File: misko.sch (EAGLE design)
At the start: 48 parts, among them IC1 MC1525TT, IC2 FT230XS, U1 ATMEGA1281-16AU, U2 SN74HCT14DR, U3 SN74LVC1G3157DBVR - BT switch, U4 SN74LVC1G3157DBVR - GPS switch, U5 TMP36GRTZ-REEL7, U6 TPS63030DSKT, U7 MCP73871-2AAI/ML

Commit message: - further work on eagle schematic
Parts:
- added C10: 0.47µF, resistor:C-EUC0805
- added C11, C13: 10µF, resistor:C-EUC0805
- added G1: CR2450V, battery:CR2450V
- added NTC: 10k, rcl:R-EU_R0805
- added R22, R23, R24, R25, R28, R31, R33, R34, R35: 1k, rcl:R-EU_R0805
- added R26, R29, R30: 47k, rcl:R-EU_R0805
- added R27: 270k, rcl:R-EU_R0805
- added R32: 100k, rcl:R-EU_R0805
- added S7: up, switch-omron:10-XX
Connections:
- removed net N$1: IC1.GND
- removed net N$12: U5.GND
- new net AREF: IC1.VO, U1.AREF
- new net AVCC: U1.AVCC
- new net N$11: R23.2, R24.1, U7.VPCC
- new net N$13: C13.1, G1.+, R34.1, U7.VBAT, U7.VBAT_2, U7.VBAT_SENSE
- new net N$18: R28.1, U7.THERM
- new net N$19: R27.1, R28.2
- new net N$20: NTC.1, R27.2
- new net N$22: R31.1, U7.PROG1
- new net N$23: R32.1, U7.PROG3
- new net RESET: U1.~RESET
- new net XTAL1: U1.XTAL1
- new net XTAL2: U1.XTAL2
- net BAT_A_PIN: now also R33.1, R34.2, U1.PF2_(ADC2); no longer U1.PF3_(ADC3)
- net GND: now also C11.2, C13.2, G1.-, IC1.GND, NTC.2, R24.2, R31.2, R32.2, R33.2, R35.2, U5.GND, U7.VSS, U7.VSS_2
- net MCP73871_CHARGE_STATUS_1_PIN: now also R30.2, U7.STAT1/*LBO
- net MCP73871_CHARGE_STATUS_2_PIN: now also R29.2, U7.STAT2
- net MCP73871_POWER_GOOD_PIN: now also R26.2, U7.*PG
- net VCC: now also C11.1, R23.1, R25.1, R26.1, R29.1, R30.1, U7.*TE, U7.CE, U7.IN, U7.IN_2, U7.OUT, U7.OUT_2, U7.PROG2, U7.SEL
- net VCC_SENSE_PIN: now also R25.2, R35.1
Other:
- note added: "Analog Switch"
- note added: "Motherboard"
- note added: "Power Supply"
- note added: "Temperature Sensor"
- note added: "Vcc Measurement"
- note added: "Voltage Reference"
- moved on the sheet: C1, IC1, LED1, LED2, R1, R5, U1, U3, U4, U5, U6, U7

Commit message: - further porting of schematic to eagle
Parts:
- removed S7: up, switch-omron:10-XX
- added C12: 4.7µF, resistor:C-EUC0805
- added C14: 0.1µF, resistor:C-EUC0805
- added S8: SWS001, smd-special:SWS001
- C10: value 0.47µF -> 10µF
- R22, R33, R34: value 1k -> 150k
- R23: value 1k -> 100k
- R24: value 1k -> 270k
- R25, R35: value 1k -> 200k
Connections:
- new net N$1: R22.1, S8.1, U6.EN
- new net N$12: U7.IN
- new net N$15: U7.SEL
- new net N$24: U7.PROG2
- new net N$25: U7.*TE
- new net N$26: U7.CE
- new net N$28: R17.1, R20.1, S5.S, S5.S1
- new net N$29: R16.1, R19.1, S6.S, S6.S1
- new net N$30: R18.1, R21.1, S4.S, S4.S1
- new net VBAT: C11.1, C12.2, S8.2, U6.PS/SYNC, U6.VIN, U6.VINA, U7.OUT, U7.OUT_2
- net 5V0: now also R23.1, U7.IN_2
- net GND: now also C10.1, C12.1, C14.2, R22.2, U6.GND, U6.PGND; no longer R16.1, R17.1, R18.1, R19.1, R21.1, S4.S, S4.S1, S5.S, S5.S1, S6.S, S6.S1
- net VCC: now also C10.2, C14.1, U6.FB, U6.VOUT; no longer C11.1, R23.1, U7.*TE, U7.CE, U7.IN, U7.IN_2, U7.OUT, U7.OUT_2, U7.PROG2, U7.SEL
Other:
- note added: "Power Supply - Buck/Boost Regulator"
- note added: "Power Supply - Power Path Controller"
- note added: "USB to Serial"
- note removed: "Power Supply"
- moved on the sheet: C1, C10, C11, C13, C2, C3, C4, C5, C6, C7, C8, C9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

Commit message: - further work on eagle schematic
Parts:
- removed C1: (no value), resistor:C-EUC1206
- removed G1: CR2450V, battery:CR2450V
- removed R1: (no value), resistor:R-EU_R1206
- added CN1: (no value), SIM800C:JST_2PIN-SMT
- added G2: CR2450V, battery:CR2450V
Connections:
- removed net N$13: C13.1, G1.+, R34.1, U7.VBAT, U7.VBAT_2, U7.VBAT_SENSE
- removed net N$24: U7.PROG2
- removed net N$25: U7.*TE
- removed net N$26: U7.CE
- new net VBAT+: C13.1, CN1.1, G2.+, R34.1, U7.VBAT, U7.VBAT_2, U7.VBAT_SENSE
- net GND: now also CN1.2, G2.-; no longer G1.-
- net N$15: now also U7.*TE, U7.CE, U7.PROG2
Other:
- moved on the sheet: R29, R30

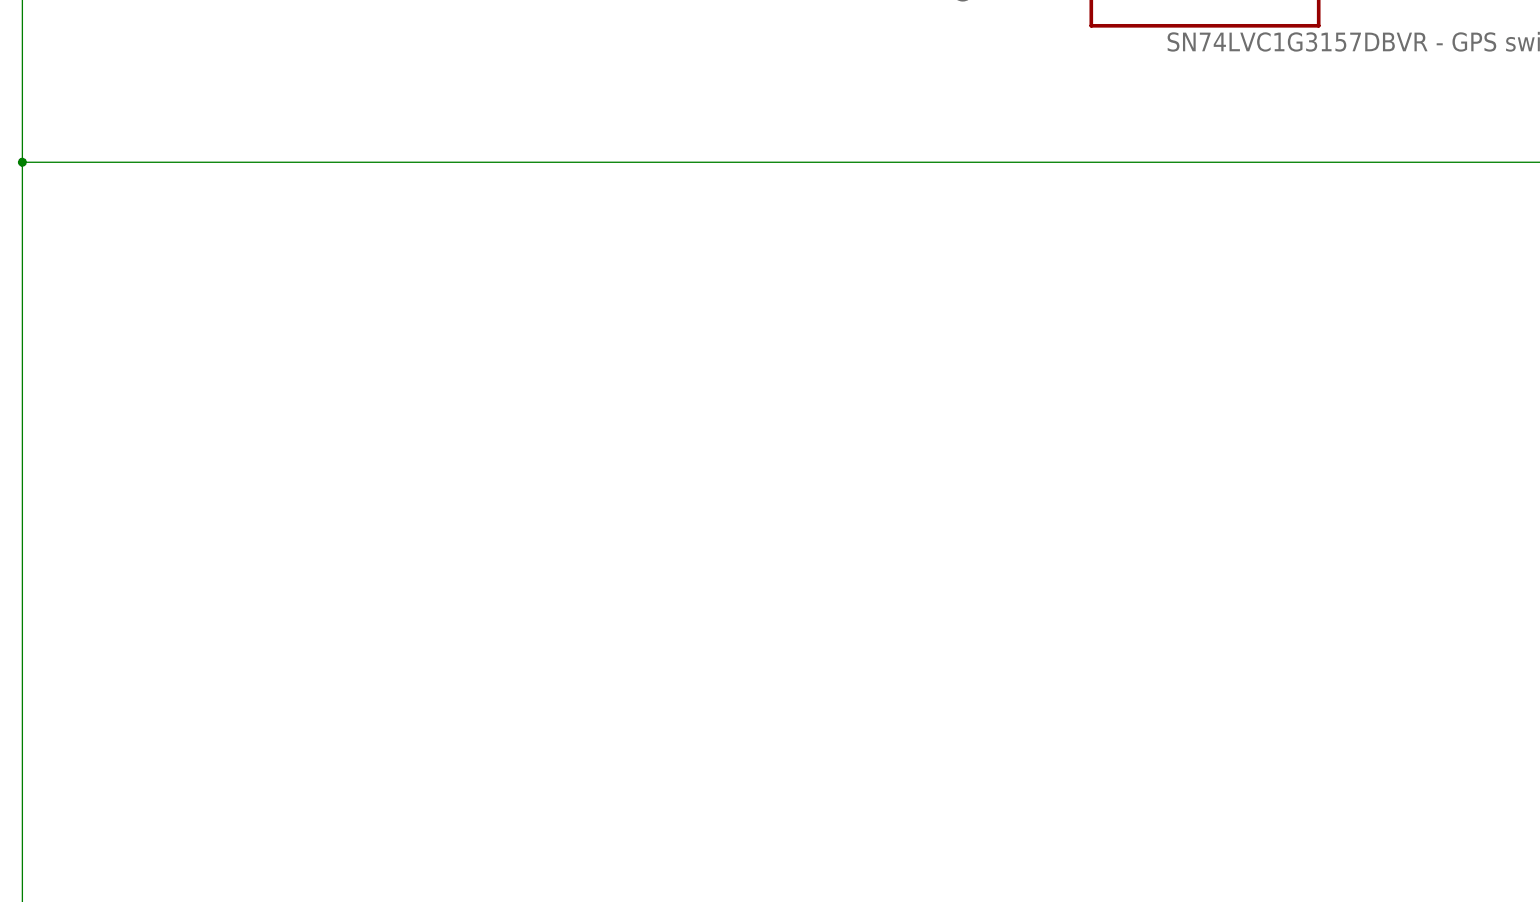
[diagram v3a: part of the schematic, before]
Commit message: - added ADXL345 Accelerometer.lbr, WIP
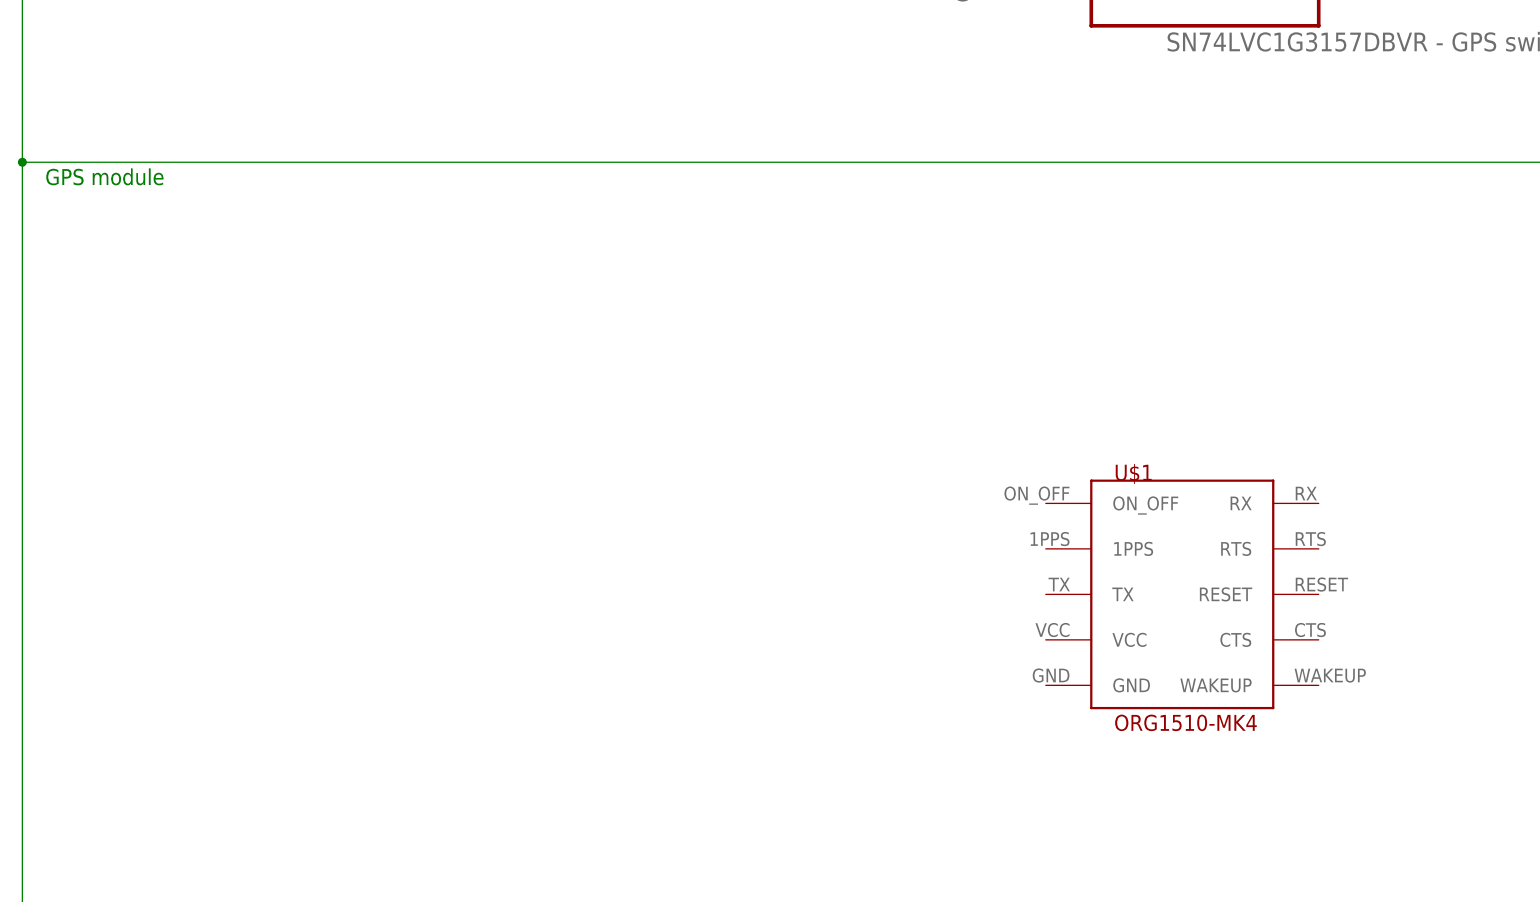
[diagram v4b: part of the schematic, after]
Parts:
- added U$1: ORG1510-MK4, ORG1510-MK4 GPS module:ORG1510-MK4
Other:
- note added: "GPS module"
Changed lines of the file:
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@@
 <setting verticaltext="up"/>
 </settings>
-<grid distance="0.1" unitdist="inch" unit="inch" style="lines" multiple="1" display="no" altdistance="0.01" altunitdist="inch" altunit="inch"/>
+<grid distance="0.1" unitdist="inch" unit="inch" style="lines" multiple="1" display="yes" altdistance="0.01" altunitdist="inch" altunit="inch"/>
 <layers>
 <layer number="1" name="Top" color="4" fill="1" visible="no" active="no"/>
@@
 <part name="CN1" library="SIM800C" deviceset="JST_2PIN" device="-SMT"/>
 <part name="G2" library="battery" deviceset="CR2450V" device=""/>
+<part name="U$1" library="ORG1510-MK4 GPS module" deviceset="ORG1510-MK4" device=""/>
 </parts>
 <sheets>
@@
 <text x="134.62" y="553.72" size="1.778" layer="91">Power Supply - Power Path Controller</text>
 <text x="5.08" y="320.04" size="1.778" layer="91">USB to Serial</text>
+<text x="2.54" y="99.06" size="1.778" layer="91">GPS module</text>
 </plain>
 <instances>
@@
 <instance part="CN1" gate="G$1" x="320.04" y="510.54"/>
 <instance part="G2" gate="1" x="274.32" y="480.06" rot="R90"/>
+<instance part="U$1" gate="G$1" x="119.38" y="40.64"/>
 </instances>
 <busses>

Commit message: - added two datasheets
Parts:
- added ANT1: (no value), discrete:ANTENNA
- added C1: 1µF, resistor:C-EUC1206
- added C15: 18pF, resistor:C-EUC1206
- added C16: 18pF, rcl:C-EUC0805
- added C17, C21, C26: 0.1µF, rcl:C-EUC0805
- added C18: 1F, rcl:C-EUC0805
- added C19, C20: 100µF, rcl:C-EUC0805
- added C22, C29: 0.1µF, resistor:C-EUC0805
- added C23, C24: 15pF, resistor:C-EUC0805
- added C25, C27, C28: 10µF, rcl:C-EUC0805
- added C30: 100nF, resistor:C-EUC1206
- added D1: 1N4148, Diode2:1N4148
- added IC3: LTC4425, LTC4425 Supercap Charger:LTC4425
- added IC4: FM25W256-SOIC, FM25W256 FERAM:FM25W256-SOIC
- added IC5: (no value), 74HCT1G32GW:74HCT1G32GW-DC
- added L1: DJNR6045-100-S, DJNR6045-100S Power Inductor:DJNR6045-100-S
- added L2: 33µH, rcl:L-US
- added L3: 1.5µH, inductor-neosid:MS50
- added LED4, LED6: red, led:LEDSML1206
- added LED5: green, led:LEDSML1206
- added Q1: FDN304P, transistor-power:N-HEXFET-2D_SOT232-IRLL014N
- added Q2: 8MHz, crystal:CRYTALHC33U-V
- added R1: 220, resistor:R-EU_R1206
- added R36, R42, R43, R44: 10k, resistor:R-EU_R1206
- added R37, R38: 100k, resistor:R-EU_R1206
- added R39, R41, R48, R50, R52: 1k, resistor:R-EU_R1206
- added R40: 46k, resistor:R-EU_R1206
- added R45, R46: 270k, rcl:R-EU_R0805
- added R47: 47k, rcl:R-EU_R0805
- added R49: 4.7k, rcl:R-EU_R0805
- added R51: 47k, resistor:R-EU_R1206
- added S7: left, switch-omron:10-XX
- added SJ1, SJ2: (no value), jumper:SJW
- added SV1: (no value), con-lstb:MA05-2
- added SV2: (no value), con-lstb:MA04-1
- added U$2: ORG1510-MK4, ORG1510-MK4 GPS module:ORG1510-MK4
- added U$3: RN-42, EN42-I Bluetooth Module:RN-42
- added U$4: ADXL345, ADXL345 Accelerometer:ADXL345
- added X1: MINI-USB_4P-32005-101, con-cypressindustries:MINI-USB_4P-32005-101
- added X2: SIM-CARD_496191611, con-molex:SIM-CARD_496191611
- added X3: SDBMF, farnell:SDBMF
- C6: value 0.1µF -> 10µF; device resistor:C-EUC0805 -> rcl:C-EUC0805
- LED1: value (none) -> blue
- R14: value 21 -> 100k; device rcl:R-EU_R0805 -> resistor:R-EU_R1206
- R15: value 21 -> 1k; device rcl:R-EU_R0805 -> resistor:R-EU_R1206
- U$1: value ORG1510-MK4 -> SIM800; device ORG1510-MK4 GPS module:ORG1510-MK4 -> SIM800 GPRS Module:SIM800
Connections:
- removed net N$12: U7.IN
- removed net N$2: U4.GND
- new net BLUETOOTH_RX: U$3.UART_RX, U3.A
- new net GPS_RX: C15.2, U$2.RX, U3.B1
- new net N$13: R1.2
- new net N$24: IC3.PFI, R37.2, R38.1
- new net N$25: IC3.PROG, R40.2
- new net N$26: IC3.EN, R39.2
- new net N$27: IC3.PFI_RET, R37.1
- new net N$31: C22.2, D1.A, R47.1
- new net N$32: C19.2, C20.2, IC3.VMID
- new net N$33: R42.2, U$3.GPIO7
- new net N$34: C6.2, LED1.A, Q1.D, U$3.VCC
- new net N$35: LED1.C, R41.2
- new net N$36: R14.1, U$3.GPIO4
- new net N$38: SJ1.2, U$3.GPIO6
- new net N$39: SJ2.2, U$3.RESET
- new net N$40: IC5.Y, U$4.SDA
- new net N$41: LED5.C, R46.2
- new net N$43: LED4.C, R45.2
- new net N$44: LED6.A, R50.2
- new net N$45: R50.1, U$1.NETLIGHT
- new net N$46: C27.2, R52.1, U$1.GSM_ANT
- new net N$47: U$1.GND10, U$1.GND9
- new net N$48: U$1.GND6, U$1.GND7
- new net N$49: ANT1.1, C28.2, R52.2
- new net N$51: R48.1, U$1.VDD_EXT
- new net N$53: L3.2, U6.L1
- new net N$54: L3.1, U6.L2
- new net SIM_CLOCK: U$1.SIM_CLK
- new net SIM_DATA: C25.1, U$1.SIM_DATA
- new net SIM_DETECT: R48.2, U$1.SIM_DET
- new net SIM_RESET: U$1.SIM_RST
- new net SIM_VDD: U$1.SIM_VDD
- new net VGPS: C1.1, C18.2, IC3.VOUT1, IC3.VOUT2, U$2.VCC
- new net VUSB: L1.2, X1.1
- net 5V0: now also C30.2, L1.1, SV2.4, U7.IN
- net ADXL345_INT1_INTERRUPT_PIN: now also U$4.INT1
- net AVCC: now also C29.1, IC1.VIN, L2.1
- net BLUETOOTH_TX: now also U$3.UART_TX
- net BLUETOOTH_WAKEUP_PIN: now also Q1.G, R15.1
- net GND: now also C1.2, C15.1, C16.2, C17.2, C18.1, C20.1, C21.1, C22.1, C23.1, C24.1, C25.2, C26.1, C27.1, C28.1, C30.1, C6.1, IC3.GND, IC4.GND, LED6.C, R14.2, R36.2, R41.1, R42.1, S7.P, S7.P1, SV1.10, SV1.2, SV2.1, U$1.GND2, U$1.GND3, U$1.GND4, U$1.GND8, U$2.GND, U$3.GND1, U$3.GND2, U$3.GND3, U$3.GND4, U$3.GPIO3, U$4.GND$1, U$4.GND$2, U$4.GND$3, U4.GND, X1.4
- net GPS_GREEN_LED_PIN: now also R46.1
- net GPS_POWER_CTL_PIN: now also R1.1, R36.1, U$2.ON_OFF
- net GPS_RED_LED_PIN: now also R45.1
- net GPS_SW_SERIAL_TX: no longer U3.B1
- net GPS_TX: now also C16.1, U$2.TX
- net GPS_WAKEUP_PIN: now also U$2.WAKEUP
- net I2C_SCL_PIN: now also SV2.3
- net I2C_SDA_PIN: now also SV2.2
- net JTAG_TCL_PIN: now also SV1.1
- net JTAG_TDI_PIN: now also SV1.9
- net JTAG_TDO_PIN: now also SV1.3
- net JTAG_TMS_PIN: now also SV1.5
- net RESET: now also R47.2, R49.2, S7.S, S7.S1, SV1.6
- net SIM800C_CTS_PIN: now also U$1.UART1_CTS
- net SIM800C_POWER_PIN: now also R51.1, U$1.PWRKEY
- net SIM800C_RX_PIN: now also U$1.UART1_TXD
- net SIM800C_STATUS_PIN: now also U$1.STATUS
- net SIM800C_TX_PIN: now also U$1.UART1_RXD
- net SPI_FRAM_SS_PIN: now also IC4.!CS!, R44.1
- net SPI_MISO_PIN: now also IC4.SO, U$4.SDO
- net SPI_MOSI_PIN: now also IC4.SI, IC5.B
- net SPI_SCK_PIN: now also IC4.SCK, U$4.SCL
- net SPI_SS_ADXL345_PIN: now also IC5.A, R43.2, U$4.!CS!
- net USB_D+: now also X1.3
- net USB_D-: now also X1.2
- net VBAT: now also C26.2, R51.2, U$1.VBAT1, U$1.VBAT2, U$1.VRTC
- net VCC: now also C17.1, C19.1, C21.2, C29.2, D1.C, IC3.FB, IC3.SEL, IC3.VCC1, IC3.VCC2, IC4.!HOLD!, IC4.!WP!, IC4.VCC, LED4.A, LED5.A, Q1.S, R15.2, R38.2, R39.1, R40.1, R43.1, R44.2, R49.1, SV1.4, U$4.VDDIO, U$4.VS; no longer IC1.VIN
- net XTAL1: now also C23.2, Q2.1
- net XTAL2: now also C24.2, Q2.2
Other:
- note added: "ADXL345 Accelerometer"
- note added: "AVCC Circuit"
- note added: "Bluetooth Module"
- note added: "FERAM Module"
- note added: "I2C Connector"
- note added: "JTAG Header"
- note added: "Oscillator Circuit"
- note added: "Reset Circuit"
- note added: "SPI Bus"
- note added: "Status LEDs"
- note added: "Supercap Charger"
- moved on the sheet: C6, IC1, LED1, R14, R15, R22, R25, R35, S8, U1

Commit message: - added new elements
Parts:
- removed ANT1: (no value), discrete:ANTENNA
- removed G2: CR2450V, battery:CR2450V
- removed Q2: 8MHz, crystal:CRYTALHC33U-V
- removed X3: SDBMF, farnell:SDBMF
- added ANT2: (no value), discrete:ANTENNASMD
- added C31: 0.1µF, rcl:C-EUC0805
- added OSCI: 8MHz, special:OSCILATOR
- added R53: 10k, resistor:R-EU_R1206
- added U$5: MICROSD_SPI_MODE, Molex SD-47309 SD Card Slot:MICROSD_SPI_MODE
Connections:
- removed net N$49: ANT1.1, C28.2, R52.2
- new net ANTENNA: ANT2.1, C28.2, R52.2
- new net N$12: C31.1, R53.2, U$5.VCC
- net GND: now also C31.2, IC5.GND, U$5.GND0, U$5.GND1, U$5.GND2, U$5.GND3; no longer G2.-
- net SD_CARD_DETECT_PIN: now also U$5.CARD_DETECT
- net SPI_MISO_PIN: now also U$5.DO
- net SPI_MOSI_PIN: now also U$5.DI
- net SPI_SCK_PIN: now also U$5.CLK
- net SPI_SS_SD_CARD_PIN: now also R53.1, U$5.CS
- net VBAT+: no longer G2.+
- net VCC: now also IC5.VCC
- net XTAL1: now also C24.2, OSCI.P$1; no longer C23.2, Q2.1
- net XTAL2: now also C23.2, OSCI.P$2; no longer C24.2, Q2.2
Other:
- note added: "SD Card Slot"

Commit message: - further work on eagle schematic
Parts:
- removed X2: SIM-CARD_496191611, con-molex:SIM-CARD_496191611
- added C32, C33, C34, C35, C36: 4.7µF, rcl:C-EUC0805
- added C37, C40: 0.1µF, rcl:C-EUC0805
- added C38: 10µF, rcl:C-EUC0805
- added C39: 4.7µF / 25V, rcl:C-EUC0805
- added D2: (no value), semicon-smd-ipc:D-SOD-80
- added L4: 33µH, rcl:L-US
- added R54, R56: 160k, resistor:R-EU_R1206
- added R55, R57: 910k, resistor:R-EU_R1206
- added U$6: V_REG_TPS61040SMD, SparkFun-PowerIC:V_REG_TPS61040SMD
- added U$7: 115Q-BCA0, 115Q-BCA0 Micro-SIM Socket:115Q-BCA0
- added X3: FH12-24S-0.5SH, con-hirose:FH12-24S-0.5SH
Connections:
- net N$4 renamed CBUS2
- net N$5 renamed CBUS1
- removed net GPS_RX: C15.2, U$2.RX, U3.B1
- removed net N$12: C31.1, R53.2, U$5.VCC
- removed net N$51: R48.1, U$1.VDD_EXT
- removed net SPI_OLED_A0_PIN: U1.(OC3B/INT4)_PE4
- removed net V_USB: R4.1, R5.2
- new net IREF: R57.2, X3-21.1
- new net N$73: D2.A, L4.1, U$6.SW
- new net N$76: C35.1, R55.1, R56.2, U$6.FB
- new net OLED_POWER_ON-OFF: R54.2, U$6.EN
- new net SPI_OLED_D/C_PIN: U1.(OC3B/INT4)_PE4, X3-10.1
- new net VCOMH: C39.2, X3-22.1
- new net VOLED: C33.2, C34.2, C35.2, C37.2, C38.2, D2.C, R55.2, X3-23.1
- net AVCC: now also C29.2, L2.2; no longer C29.1, L2.1
- net GND: now also C29.1, C32.1, C33.1, C34.1, C36.1, C37.1, C38.1, C39.1, C40.1, R54.1, R56.1, R57.1, SJ1.1, SJ2.1, U$6.GND, U$7.GND1, U$7.GND2, U$7.GND3, U$7.GND4, U$7.GND5, X3-1.1, X3-11.1, X3-12.1, X3-2.1, X3-24.1, X3-3.1, X3-6.1, X3-7.1
- net GPS_SW_SERIAL_TX: now also C15.2, U$2.RX, U3.B1
- net SIM800C_POWER_PIN: now also R48.1, U$1.VDD_EXT
- net SIM_CLOCK: now also U$7.CLK
- net SIM_DATA: now also U$7.I/O
- net SIM_DETECT: now also U$7.CD
- net SIM_RESET: now also U$7.RST
- net SIM_VDD: now also U$7.VPP
- net SPI_MOSI_PIN: now also X3-14.1
- net SPI_OLED_RESET_PIN: now also X3-9.1
- net SPI_SCK_PIN: now also X3-13.1
- net SPI_SS_OLED_PIN: now also X3-8.1
- net VCC: now also C31.1, C32.2, C36.2, C40.2, L2.1, L4.2, R53.2, U$5.VCC, U$6.VIN, X3-5.1; no longer C29.2
- net VUSB: now also R4.1, R5.2
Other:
- note added: "ER-OLED015-2W Connetor w. SSD1309"
- note added: "OLED"
- note added: "OLED Panel Power Supply"
- note added: "SIM Card Holder"
- note added: "SIM800C"
- note added: "SIM800C GPRS Module"
- moved on the sheet: ANT2, C15, C16, C18, C19, C20, C21, C25, C26, C27, C28, C29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

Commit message: - crude positioning of elements on approximate board size
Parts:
- added BOTTOM, TOP: FH12-24S-0.5SH, con-hirose:FH12-24S-0.5SH
- added L5: DJNR6045-100-S, DJNR6045-100S Power Inductor:DJNR6045-100-S
- added SUPERCAP: 1F, capacitor-wima:C5/2.5
- C18: value 1F -> 100nF; device rcl:C-EUC0805 -> resistor:C-EUC1206
- CN1: value (none) -> LiPo Battery
- NTC: device rcl:R-EU_R0805 -> rcl:R-EU_0204/5
- S7: value left -> RESET
- S8: value SWS001 -> POWER_SWITCH
- renumbered LED1 to BT_LED, LED2 to USB_TX_LED, LED3 to USB_RX_LED, LED4 to GPS_RED_LED, LED5 to GPS_GREEN_LED, LED6 to GPRS_LED
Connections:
- new net N$100: BOTTOM-23.1
- new net N$12: IC2.RXD, R3.2
- new net N$5: L5.1, SV2.4
- new net N$86: BOTTOM-21.1
- new net N$87: BOTTOM-22.1
- new net N$90: TOP-23.1
- new net N$91: TOP-22.1
- new net N$92: TOP-21.1
- net 5V0: now also C18.2, L5.2; no longer SV2.4
- net ANALOG_SW_CTRL_PIN: now also BOTTOM-13.1, TOP-13.1
- net GND: now also BOTTOM-1.1, BOTTOM-24.1, SUPERCAP.1, TOP-1.1, TOP-24.1, U$5.GND4; no longer U$5.GND0
- net GPS_GREEN_LED_PIN: now also BOTTOM-10.1, BOTTOM-12.1, TOP-10.1, TOP-12.1
- net GPS_POWER_CTL_PIN: now also BOTTOM-18.1, TOP-18.1
- net GPS_RED_LED_PIN: now also BOTTOM-11.1, BOTTOM-9.1, TOP-11.1, TOP-9.1
- net GPS_SW_SERIAL_RX: now also BOTTOM-19.1, TOP-19.1
- net GPS_SW_SERIAL_TX: now also BOTTOM-20.1, TOP-20.1
- net GPS_WAKEUP_PIN: now also BOTTOM-17.1, TOP-17.1
- net MENU_BLUETOOTH_POWER_TOGGLE_PIN: now also BOTTOM-4.1, TOP-4.1
- net MENU_DOWN_BUTTON_PIN: now also BOTTOM-5.1, TOP-5.1
- net MENU_GPRS_PUSH_BUTTON_PIN: now also BOTTOM-7.1, TOP-7.1
- net MENU_LEFT_BUTTON_PIN: now also BOTTOM-3.1, TOP-3.1
- net MENU_RIGHT_BUTTON_PIN: now also BOTTOM-8.1, TOP-8.1
- net MENU_UP_BUTTON_PIN: now also BOTTOM-6.1, TOP-6.1
- net PDI_UART0_CTS_PIN: now also BOTTOM-16.1, TOP-16.1
- net PDI_UART0_RX_PIN: now also BOTTOM-14.1, TOP-14.1
- net PDI_UART0_TX_PIN: now also BOTTOM-15.1, TOP-15.1; no longer IC2.RXD, R3.2
- net VCC: now also BOTTOM-2.1, TOP-2.1
- net VGPS: now also SUPERCAP.2; no longer C18.2
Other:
- moved on the sheet: C18, C29, L2, U$5
